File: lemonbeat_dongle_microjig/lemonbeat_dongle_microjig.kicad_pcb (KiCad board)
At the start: 2 copper layers, 50 x 42 mm, 20 parts, among them J1 Prog, J2 Main, J3 Si4467

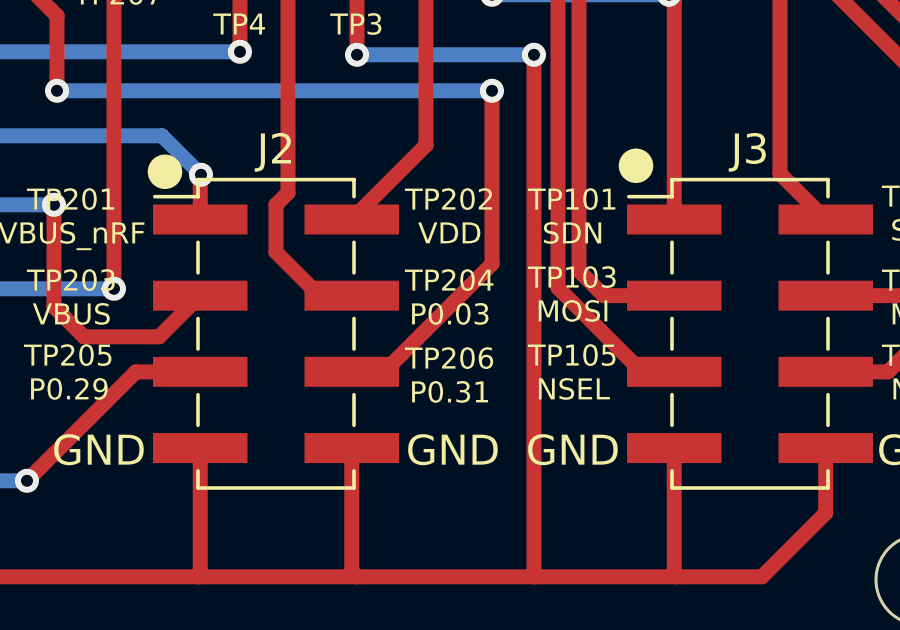
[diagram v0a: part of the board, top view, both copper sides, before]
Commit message: dongle: microjig: silk screen typo fix
TP204 is actually P0.02, not P0.03.
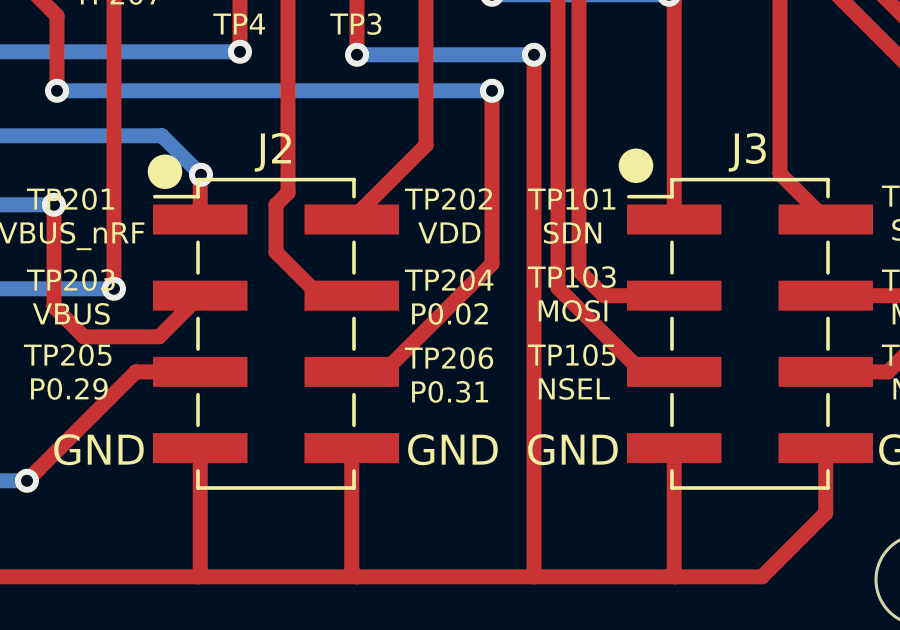
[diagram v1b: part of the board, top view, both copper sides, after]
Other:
- board text added: "TP204 P0.02"
- board text removed: "TP204 P0.03"
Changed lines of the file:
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@@
     (effects (font (size 0.7 0.7) (thickness 0.1)))
   )
-  (gr_text "TP204\nP0.03" (at 142.3 124.1) (layer "F.SilkS")
+  (gr_text "TP204\nP0.02" (at 142.3 124.1) (layer "F.SilkS")
     (effects (font (size 0.7 0.7) (thickness 0.1)))
   )

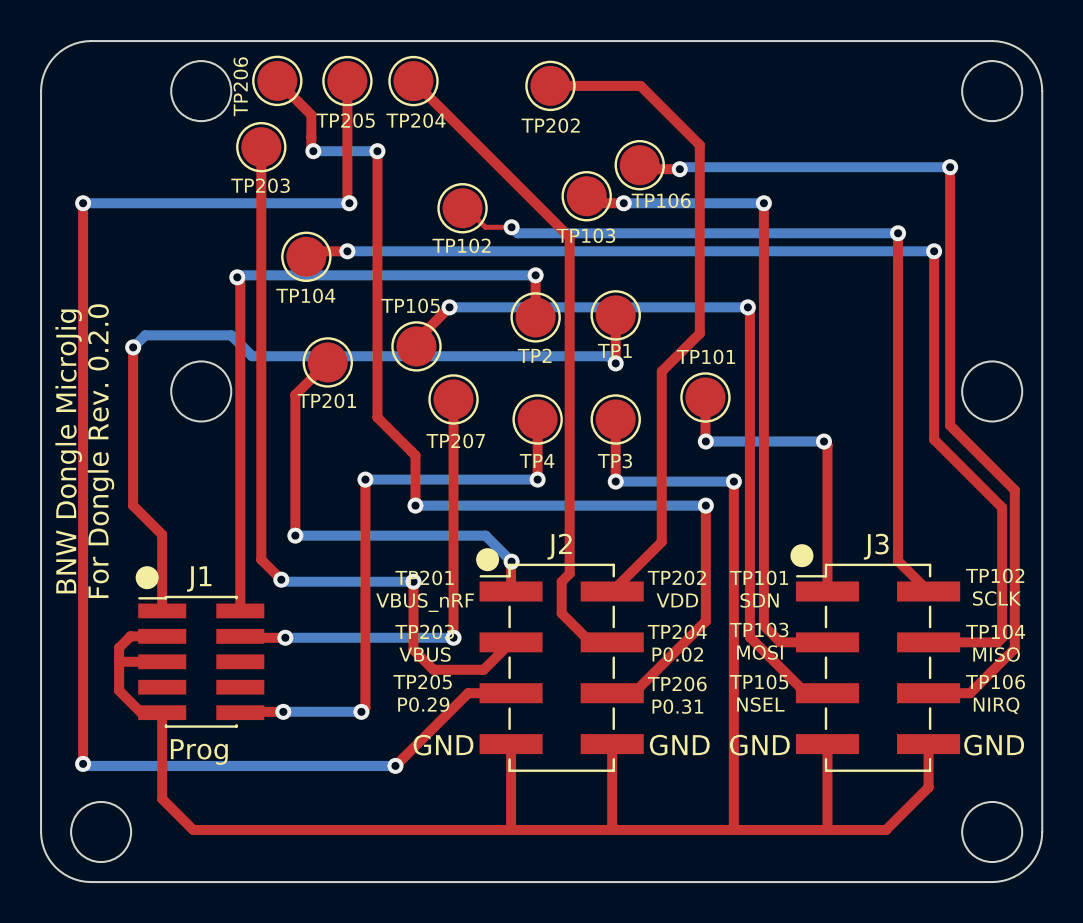
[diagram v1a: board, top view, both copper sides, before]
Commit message: dongle: PCB: move test points away from hole
- move TP203 & TP206 away from hole (dongle & microjig)
- move TP205 away from TP206 (dongle & microjig)

Having the test points further away from the holes avoids shortcuts when
using a metal case & leaves space on the microjig for a nut.
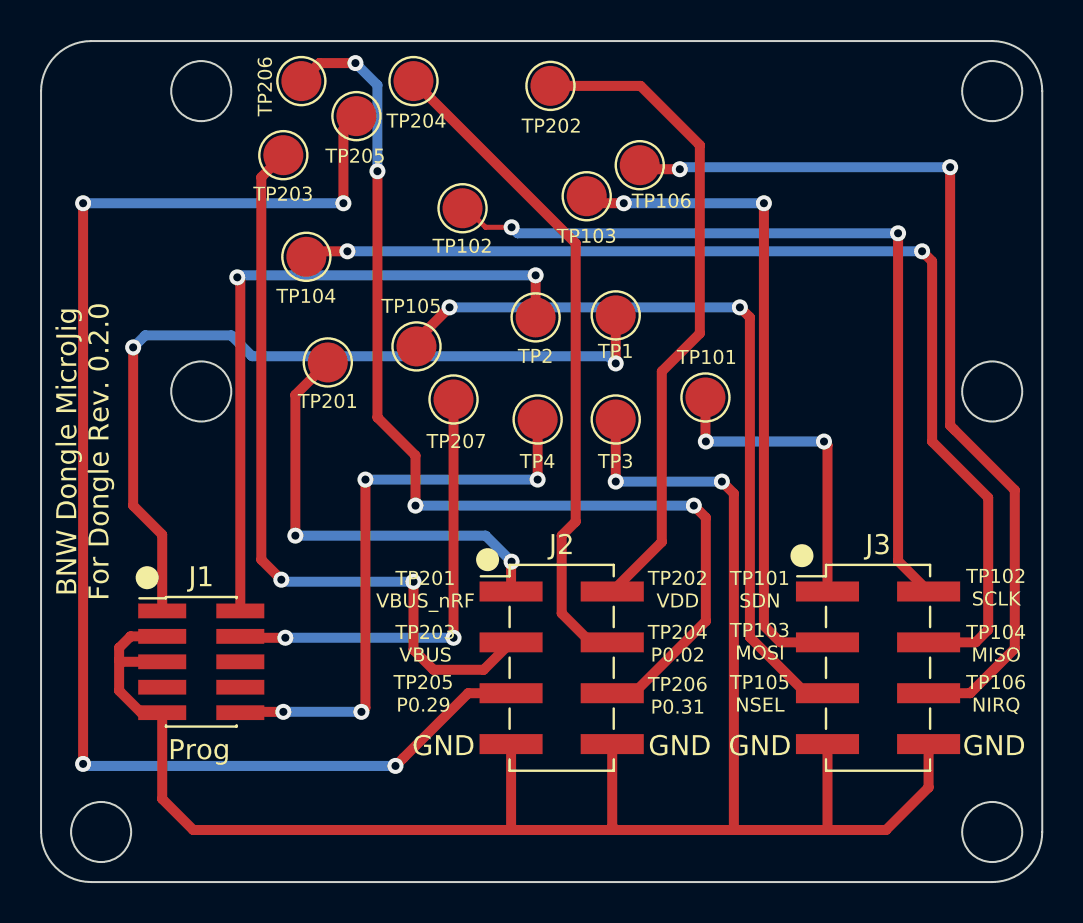
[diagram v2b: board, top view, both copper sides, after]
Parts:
- moved TP205 1.81 mm to (126.2, 97.8)
- moved TP206 1.20 mm to (123.5, 96.0)
- moved TP203 1.17 mm to (122.6, 99.7)
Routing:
- net Net-(J2-Pin_5): track 70.4 -> 68.5 mm
- net Net-(J3-Pin_4): track 55.9 -> 54.4 mm

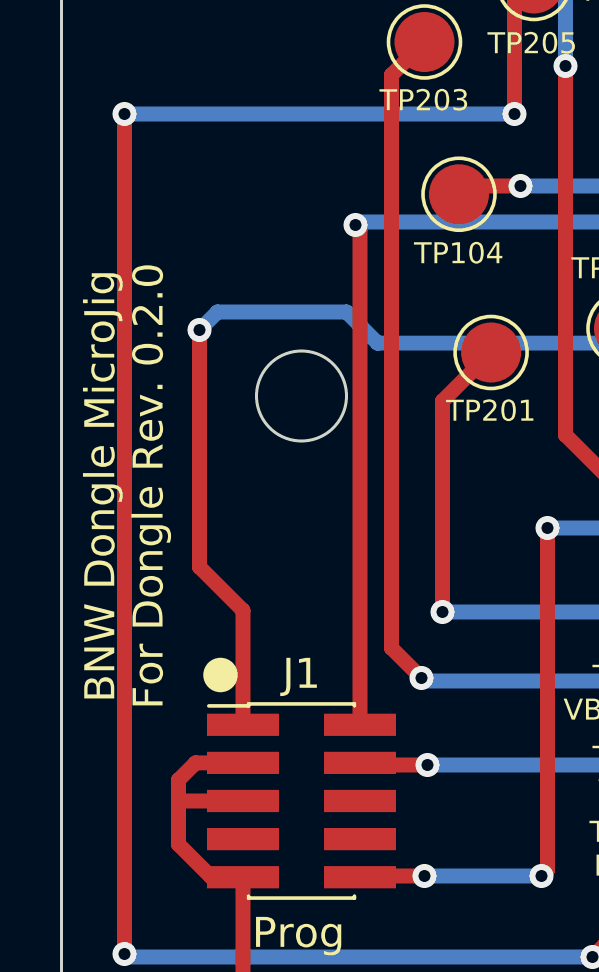
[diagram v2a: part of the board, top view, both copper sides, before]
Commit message: dongle: microjig: PCB: update silk screen "for rev. 0.3.0"
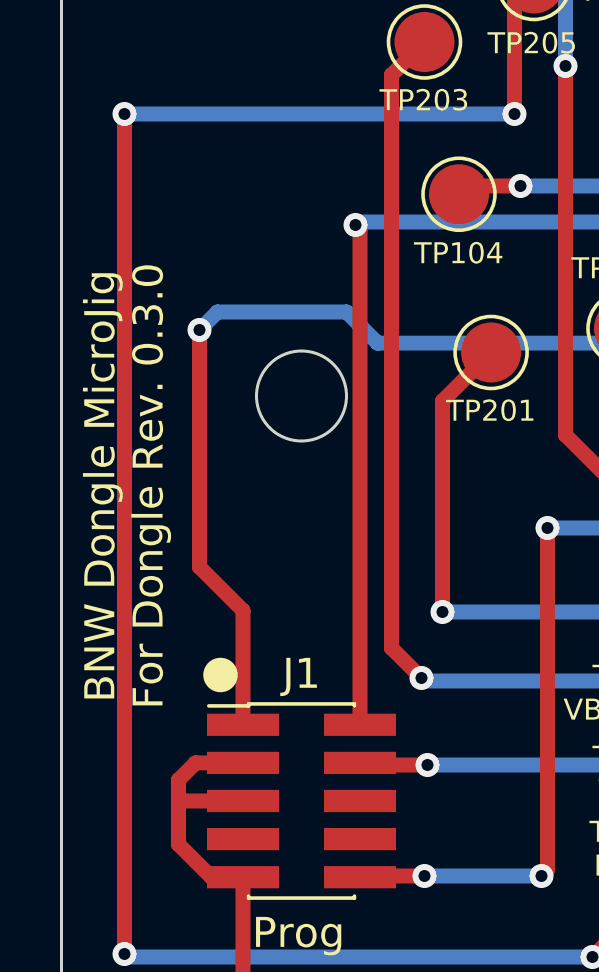
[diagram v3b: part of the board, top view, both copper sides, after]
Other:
- board text added: "BNW Dongle MicroJig For Dongle Rev. 0.3.0"
- board text removed: "BNW Dongle MicroJig For Dongle Rev. 0.2.0"
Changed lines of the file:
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@@
   (gr_line (start 113 94) (end 158 94)
     (stroke (width 0.1) (type solid)) (layer "Edge.Cuts"))
-  (gr_text "BNW Dongle MicroJig\nFor Dongle Rev. 0.2.0" (at 112.6 114.5 90) (layer "F.SilkS")
+  (gr_text "BNW Dongle MicroJig\nFor Dongle Rev. 0.3.0" (at 112.6 114.5 90) (layer "F.SilkS")
     (effects (font (size 1 1) (thickness 0.15)))
   )

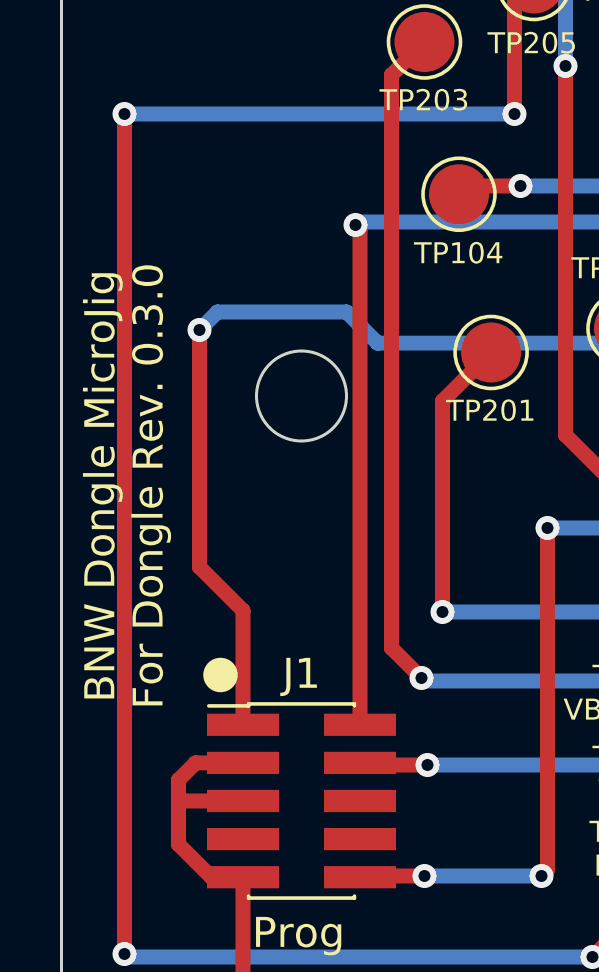
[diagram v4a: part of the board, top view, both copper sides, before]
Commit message: dongle & micro jig: increase revision to 0.4.0 everywhere
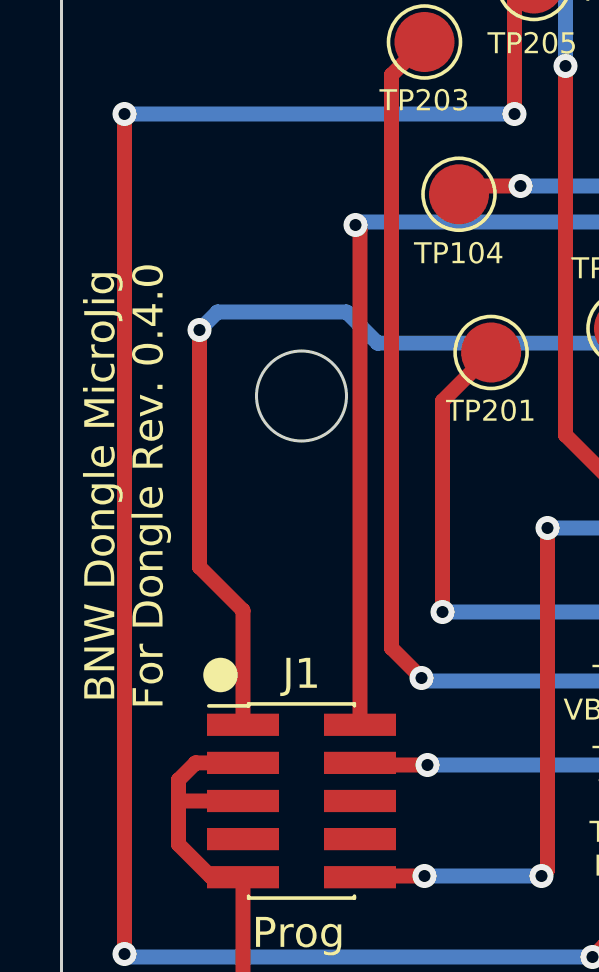
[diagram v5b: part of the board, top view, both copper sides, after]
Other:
- board text added: "BNW Dongle MicroJig For Dongle Rev. 0.4.0"
- board text removed: "BNW Dongle MicroJig For Dongle Rev. 0.3.0"
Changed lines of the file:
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@@
   (gr_line (start 113 94) (end 158 94)
     (stroke (width 0.1) (type solid)) (layer "Edge.Cuts"))
-  (gr_text "BNW Dongle MicroJig\nFor Dongle Rev. 0.3.0" (at 112.6 114.5 90) (layer "F.SilkS")
+  (gr_text "BNW Dongle MicroJig\nFor Dongle Rev. 0.4.0" (at 112.6 114.5 90) (layer "F.SilkS")
     (effects (font (size 1 1) (thickness 0.15)))
   )
